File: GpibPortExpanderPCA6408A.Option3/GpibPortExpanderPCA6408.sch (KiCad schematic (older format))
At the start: 39 parts, among them J1 DEBUG_CON_01X08, J2 GPIB_CON_9P, J3 GPIB_CON_9P, J4 SATA_PLUG_CON_14P, U1 PCA6416A

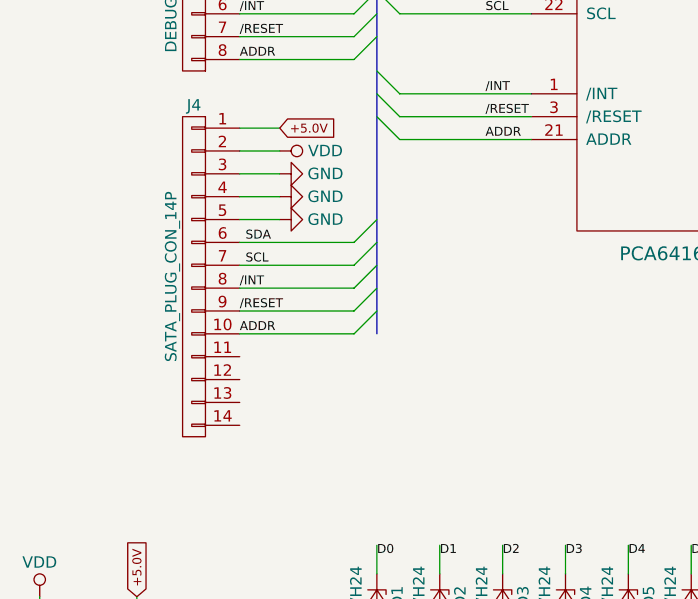
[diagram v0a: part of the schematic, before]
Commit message: Revision de PCBs + MergedPcbs
  - Se revisan PCBs
      - VikingPortExpander
      - GpibPortExpander
      - MainBoards en tres versiones
  - Se genera archivos Gerber que combina estos PCBs en un documento
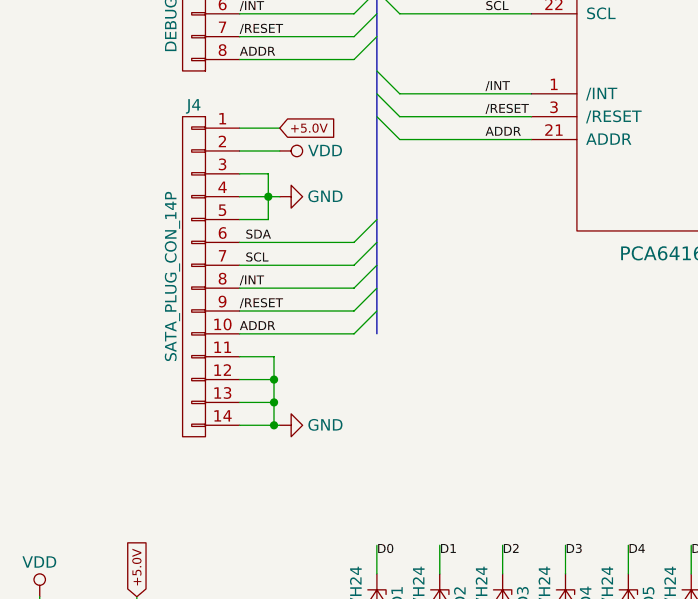
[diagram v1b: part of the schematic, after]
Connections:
- wire segments 115 -> 121
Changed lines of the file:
@@
 LIBS:74xx
 LIBS:cmos4000
-LIBS:eSim_Analog
-LIBS:eSim_Devices
-LIBS:eSim_Digital
-LIBS:eSim_Hybrid
-LIBS:eSim_Miscellaneous
-LIBS:eSim_Power
-LIBS:eSim_Sources
-LIBS:eSim_Subckt
-LIBS:eSim_User
-LIBS:eSim_Plot
-LIBS:eSim_PSpice
 LIBS:GpibPortExpanderPCA6408-cache
 EELAYER 25 0
@@
 	0    1    1    0
 $EndComp
-$Comp
-L GND #PWR026
-U 1 1 5A51AA54
-P 1825 2475
-F 0 "#PWR026" H 1825 2225 50  0001 C CNN
-F 1 "GND" V 1825 2275 50  0000 C CNN
-F 2 "" H 1825 2475 50  0000 C CNN
-F 3 "" H 1825 2475 50  0000 C CNN
-	1    1825 2475
-	0    -1   -1   0
-$EndComp
 Wire Wire Line
 	1825 2275 1650 2275
 Wire Wire Line
 	1825 2375 1650 2375
-Wire Wire Line
-	1825 2475 1650 2475
 Entry Wire Line
 	2150 2875 2250 2775
@@
 L GND #PWR?
 U 1 1 5A538127
-P 1825 2675
-F 0 "#PWR?" H 1825 2425 50  0001 C CNN
-F 1 "GND" V 1825 2475 50  0000 C CNN
-F 2 "" H 1825 2675 50  0000 C CNN
-F 3 "" H 1825 2675 50  0000 C CNN
-	1    1825 2675
+P 1825 3575
+F 0 "#PWR?" H 1825 3325 50  0001 C CNN
+F 1 "GND" V 1825 3375 50  0000 C CNN
+F 2 "" H 1825 3575 50  0000 C CNN
+F 3 "" H 1825 3575 50  0000 C CNN
+	1    1825 3575
 	0    -1   -1   0
 $EndComp
@@
 	1650 2575 1825 2575
 Wire Wire Line
-	1825 2675 1650 2675
+	1650 2475 1775 2475
+Wire Wire Line
+	1775 2475 1775 2675
+Connection ~ 1775 2575
+Wire Wire Line
+	1775 2675 1650 2675
+Wire Wire Line
+	1650 3575 1825 3575
+Wire Wire Line
+	1800 3575 1800 3275
+Wire Wire Line
+	1800 3275 1650 3275
+Connection ~ 1800 3575
+Wire Wire Line
+	1650 3375 1800 3375
+Connection ~ 1800 3375
+Wire Wire Line
+	1650 3475 1800 3475
+Connection ~ 1800 3475
 $EndSCHEMATC

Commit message: Revision de PCbs + generacion de nuevos archivos Gerber
  - Se corrigen pads de pin headers
  - Se revisan
  - MainBoard option 2
  - PortExpander MC33996.Option3
  - GpibPortExpanderPCA6408A.Option3
  - Se generan Gerber + Vistas 3D
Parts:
- J1: footprint Pin_Headers:Pin_Header_Straight_1x08_Pitch2.54mm -> CenditFootprints:DEBUG_CON_8P
- J2, J3: footprint Pin_Headers:Pin_Header_Straight_1x09_Pitch2.54mm -> CenditFootprints:GPIB_HEADER_9P
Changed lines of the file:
@@
 LIBS:74xx
 LIBS:cmos4000
+LIBS:eSim_Analog
+LIBS:eSim_Devices
+LIBS:eSim_Digital
+LIBS:eSim_Hybrid
+LIBS:eSim_Miscellaneous
+LIBS:eSim_Power
+LIBS:eSim_Sources
+LIBS:eSim_Subckt
+LIBS:eSim_User
+LIBS:eSim_Plot
+LIBS:eSim_PSpice
 LIBS:GpibPortExpanderPCA6408-cache
 EELAYER 25 0
@@
 F 0 "J1" H 1450 2075 50  0000 C CNN
 F 1 "DEBUG_CON_01X08" V 1550 1650 50  0000 C CNN
-F 2 "Pin_Headers:Pin_Header_Straight_1x08_Pitch2.54mm" H 1450 1625 50  0001 C CNN
+F 2 "CenditFootprints:DEBUG_CON_8P" H 1450 1625 50  0001 C CNN
 F 3 "" H 1450 1625 50  0001 C CNN
 	1    1450 1625
@@
 F 0 "J2" H 5375 2025 50  0000 C CNN
 F 1 "GPIB_CON_9P" V 5475 1525 50  0000 C CNN
-F 2 "Pin_Headers:Pin_Header_Straight_1x09_Pitch2.54mm" H 5375 1525 50  0001 C CNN
+F 2 "CenditFootprints:GPIB_HEADER_9P" H 5375 1525 50  0001 C CNN
 F 3 "" H 5375 1525 50  0001 C CNN
 	1    5375 1525
@@
 $EndComp
 $Comp
-L GND #PWR027
+L GND #PWR026
 U 1 1 5A34D454
 P 5075 2025
-F 0 "#PWR027" H 5075 1775 50  0001 C CNN
+F 0 "#PWR026" H 5075 1775 50  0001 C CNN
 F 1 "GND" H 5075 1875 50  0000 C CNN
 F 2 "" H 5075 2025 50  0000 C CNN
@@
 F 0 "J3" H 5350 3425 50  0000 C CNN
 F 1 "GPIB_CON_9P" V 5450 2925 50  0000 C CNN
-F 2 "Pin_Headers:Pin_Header_Straight_1x09_Pitch2.54mm" H 5350 2925 50  0001 C CNN
+F 2 "CenditFootprints:GPIB_HEADER_9P" H 5350 2925 50  0001 C CNN
 F 3 "" H 5350 2925 50  0001 C CNN
 	1    5350 2925
@@
 	5100 3325 5100 3400
 $Comp
-L GND #PWR?
+L GND #PWR027
 U 1 1 5A5380A7
 P 1825 2575
-F 0 "#PWR?" H 1825 2325 50  0001 C CNN
+F 0 "#PWR027" H 1825 2325 50  0001 C CNN
 F 1 "GND" V 1825 2375 50  0000 C CNN
 F 2 "" H 1825 2575 50  0000 C CNN
@@
 $EndComp
 $Comp
-L GND #PWR?
+L GND #PWR028
 U 1 1 5A538127
 P 1825 3575
-F 0 "#PWR?" H 1825 3325 50  0001 C CNN
+F 0 "#PWR028" H 1825 3325 50  0001 C CNN
 F 1 "GND" V 1825 3375 50  0000 C CNN
 F 2 "" H 1825 3575 50  0000 C CNN
